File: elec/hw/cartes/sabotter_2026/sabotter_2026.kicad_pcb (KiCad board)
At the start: 4 copper layers, 65 x 100 mm, 124 parts, among them J1 22272021, J10 2-1445051-3, J11 22272051, J12 22272031, J13 3-794630-6, J17 22272061, J3 USB4120-03-C, J5 22272041, J6 3-794630-4, J9 3-794630-4, SW1 PTS525 SK15 SMTR2 LFS, U1 OKI-78SR-3.3/1.5-W36H-C, U2 OKI-78SR-5/1.5-W36H-C, U3 ESP32-S3-WROOM-1, U6 TCAN1042DRQ1, U7 TCA6408ARGTR, U8 SN74LVC1T45DBV

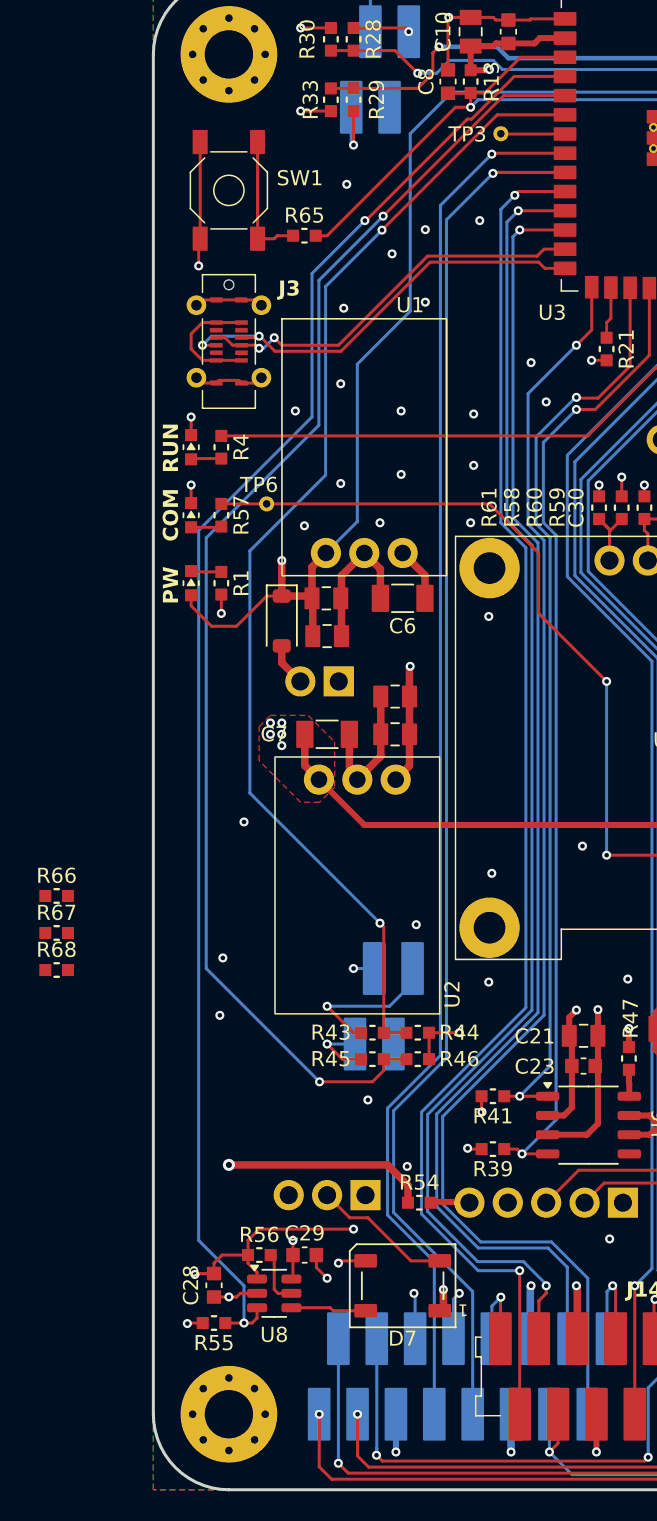
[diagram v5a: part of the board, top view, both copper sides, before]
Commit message: sabotter tof irq routed
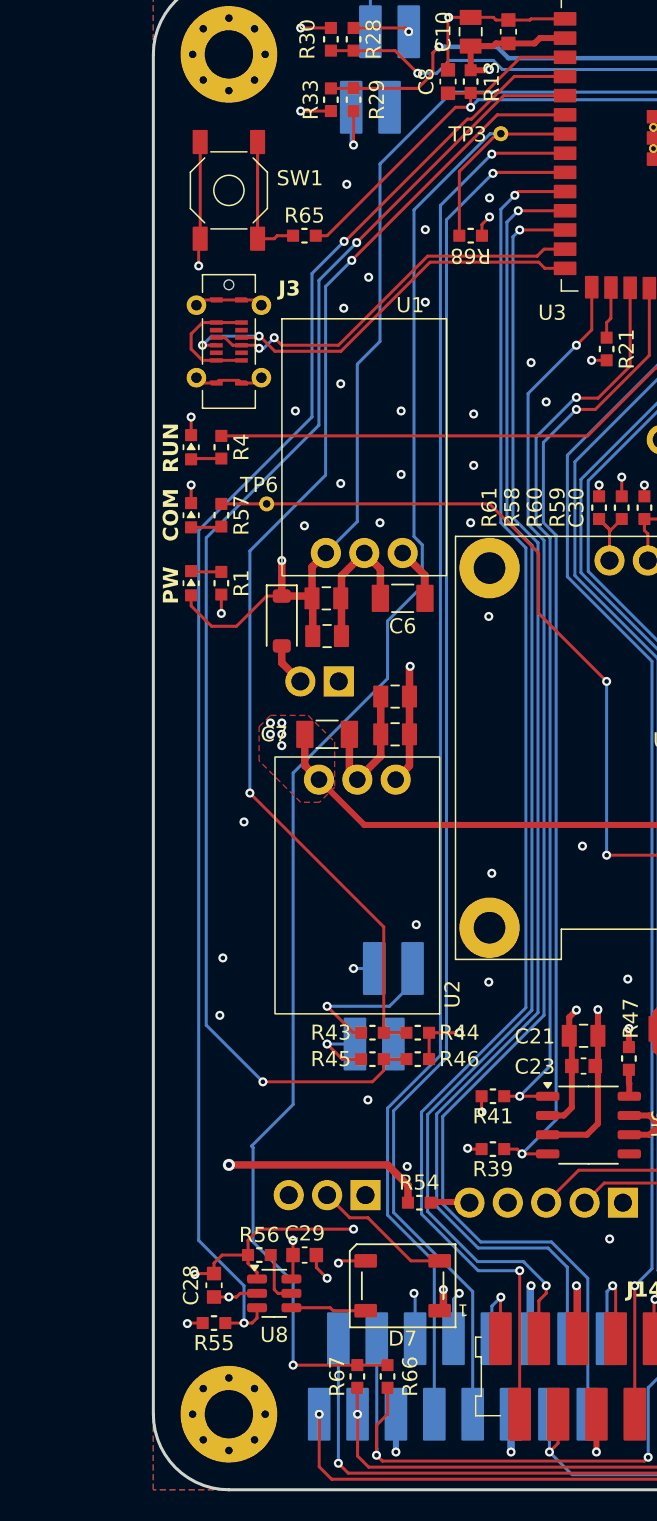
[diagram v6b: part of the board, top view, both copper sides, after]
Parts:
- moved R68 55.8 mm to (131.0, 37.0), turned to 180 degrees
- moved R66 38.6 mm to (125.5, 112.5), turned to 90 degrees
- moved R67 35.5 mm to (123.5, 112.5), turned to 90 degrees
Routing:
- net /motors/tof_irq_3v3: track 4.26 -> 108.9 mm, vias 0 -> 1
- net /motors/irq0_3v3: track 45.8 -> 50.5 mm
- net /interfaces/rx_from_prop_3v3: track 87.4 -> 89.6 mm
- net /motors/irq1_3v3: track 34.1 -> 35.8 mm
- net +3V3: track 91.9 -> 93.4 mm, vias 27 -> 28

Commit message: sabotter corrections wip
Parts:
- added SW2: SLW-713515-2A-SMT-TR, cocotter_others:SLW-713515-2A-SMT-TR, F.Cu at (122.0, 34.0)
- added SW3: SLW-713515-2A-SMT-TR, cocotter_others:SLW-713515-2A-SMT-TR, F.Cu at (170.0, 79.2)
- moved R65 63.2 mm to (164.6, 81.8), turned to 180 degrees
- moved C25 8.61 mm to (169.2, 100.2), turned to 0 degrees
- moved R49 6.64 mm to (169.2, 101.8), turned to 180 degrees
- moved R51 4.00 mm to (169.3, 104.0), turned to 180 degrees
- moved C26 2.94 mm to (169.3, 105.5), turned to 0 degrees
- moved J9 1.25 mm to (162.2, 102.5)
- moved J13 1.00 mm to (149.5, 102.5)
- moved J11 0.50 mm to (135.5, 101.0)
- moved J12 0.50 mm to (122.0, 100.5)
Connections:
- R65 pad 1: Net-(SW1-2) -> Net-(R65-Pad1)
- R65 pad 2: /uc/EN_ESP32_3v3 -> /interfaces/color_select_3v3
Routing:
- net /scl_tof_3v3: track 144.4 -> 136.6 mm
- net /interfaces/ctc_right_3v3: track 17.0 -> 12.9 mm
- net /interfaces/starting_cord_3v3: track 36.7 -> 40.0 mm
- net /motors/DIR_MOT2_3V3: track 84.0 -> 86.7 mm
- net Net-(R65-Pad1): track 0.00 -> 2.00 mm
- net /motors/PWM_MOT2_3V3: track 87.8 -> 89.7 mm
- net /interfaces/ws2812_data_3v3: track 98.9 -> 100.6 mm
- net /interfaces/rx_from_prop_3v3: track 89.6 -> 91.2 mm
- net /interfaces/tx_to_prop_3v3: track 77.2 -> 78.6 mm
- net /interfaces/color_select_3v3: track 30.3 -> 31.6 mm
- net /brake_mot_3v3: track 55.8 -> 57.1 mm
- net /sda_tof_3v3: track 136.3 -> 137.3 mm
- net /interfaces/reset_tof_3v3: track 16.4 -> 17.2 mm
- net /interfaces/enable_tof_3v3: track 14.9 -> 15.5 mm
- net /interfaces/ctc_left_3v3: track 18.3 -> 17.8 mm
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
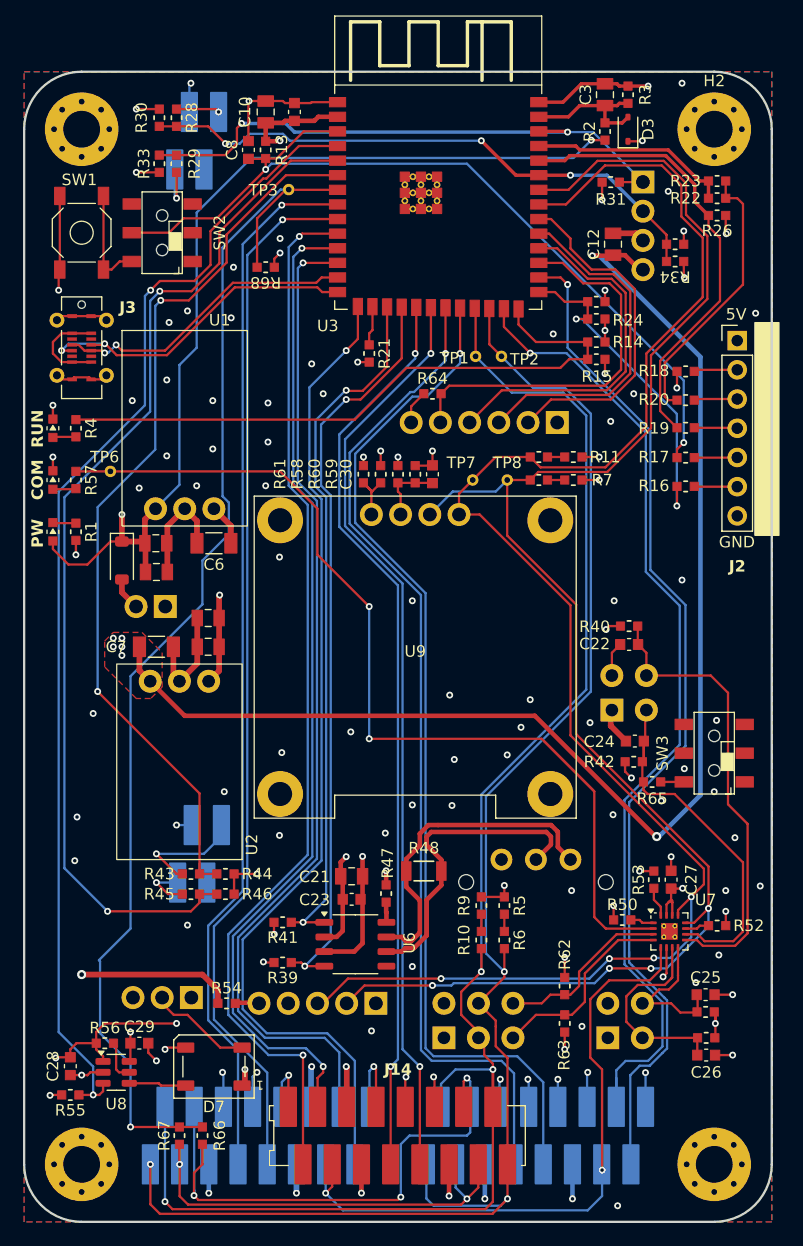
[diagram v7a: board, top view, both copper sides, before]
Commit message: sabotter upodate : switch added to uc reset and color selection
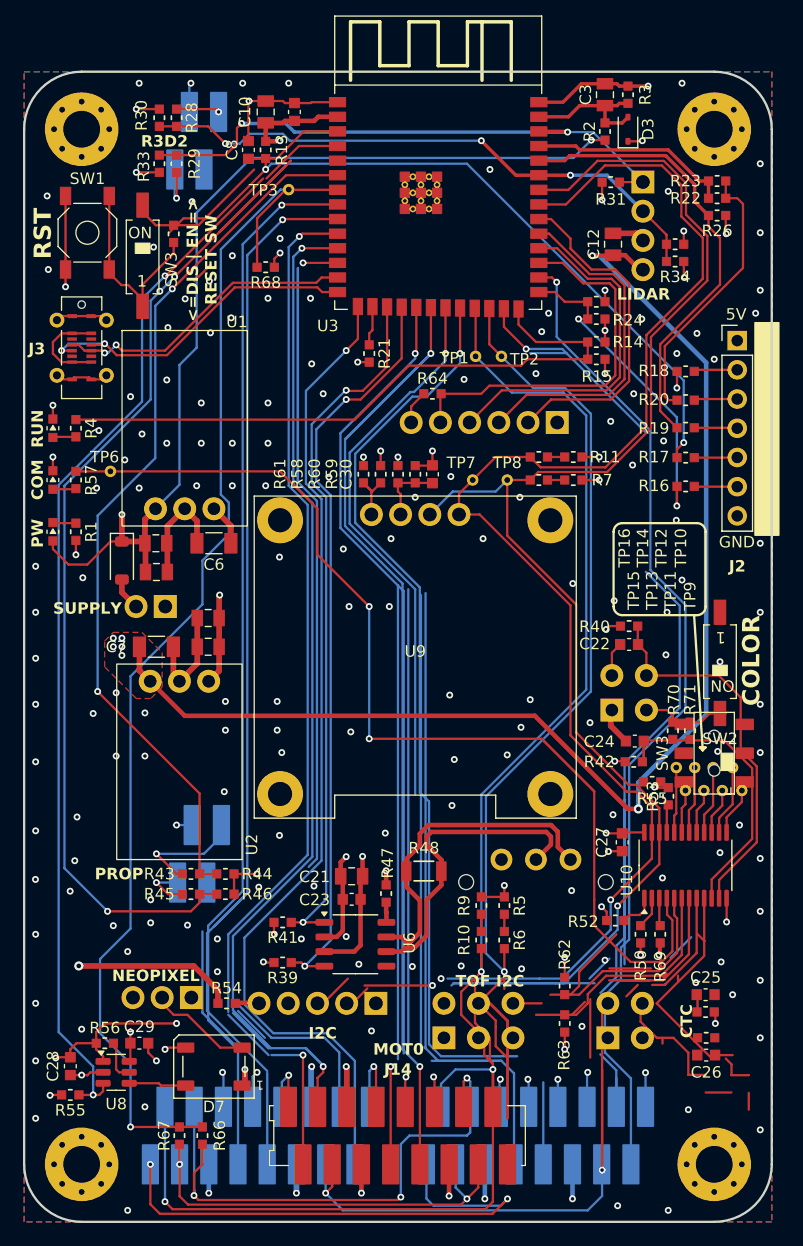
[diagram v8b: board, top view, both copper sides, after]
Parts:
- removed U7: TCA6408ARGTR, cocotter_ic:VQFN-16-1EP_3x3mm_P0.5mm_EP1.1x1.1mm
- added R65: 0R, cocotter_resistor:r0603_reflow, F.Cu at (123.0, 34.1)
- added R69: 0R, cocotter_resistor:r0603_reflow, F.Cu at (165.3, 95.0)
- added R70: 0R, cocotter_resistor:r0603_reflow, F.Cu at (166.4, 77.3)
- added R71: 0R, cocotter_resistor:r0603_reflow, F.Cu at (167.9, 77.3)
- added SW3: DSIC01LSGER, cocotter_others:DIP_SW_SMD-1P, F.Cu at (120.3, 36.0)
- added TP10: TestPoint, cocotter_others:testpoint-THT-0.5mm, F.Cu at (171.6, 80.5)
- added TP11: TestPoint, cocotter_others:testpoint-THT-0.5mm, F.Cu at (170.7, 82.5)
- added TP12: TestPoint, cocotter_others:testpoint-THT-0.5mm, F.Cu at (169.9, 80.5)
- added TP13: TestPoint, cocotter_others:testpoint-THT-0.5mm, F.Cu at (169.1, 82.5)
- added TP14: TestPoint, cocotter_others:testpoint-THT-0.5mm, F.Cu at (168.3, 80.5)
- added TP15: TestPoint, cocotter_others:testpoint-THT-0.5mm, F.Cu at (167.5, 82.5)
- added TP16: TestPoint, cocotter_others:testpoint-THT-0.5mm, F.Cu at (166.7, 80.5)
- added TP9: TestPoint, cocotter_others:testpoint-THT-0.5mm, F.Cu at (172.4, 82.5)
- added U10: PCA9535PW, Package_SO:TSSOP-24_4.4x7.8mm_P0.65mm, F.Cu at (167.5, 89.0)
- R50: value 91k 1% -> 0R
- SW1: footprint cocotter_others:PTS525 SK15 SMTR2 LFS -> cocotter_others:PTS525
- SW2: value SLW-713515-2A-SMT-TR -> DSIC01LSGER; footprint cocotter_others:SLW-713515-2A-SMT-TR -> cocotter_others:DIP_SW_SMD-1P
- moved SW2 61.2 mm to (170.5, 71.4), turned to 180 degrees
- moved R52 8.86 mm to (161.4, 93.8), turned to 0 degrees
- moved R53 7.36 mm to (166.0, 83.0)
- moved C27 5.35 mm to (162.0, 87.0), turned to -90 degrees
- moved R50 2.03 mm to (163.6, 95.0), turned to -90 degrees
- moved SW1 0.50 mm to (115.5, 34.0)
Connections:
- J6 pad 2: /interfaces/color_select_3v3 -> Net-(J6-Pad2)
- R50 pad 1: +3V3 -> Net-(U10-A1)
- R50 pad 2: Net-(U7-~{RESET}) -> GND
- SW2 pad 1: Net-(SW1-2) -> GND
- SW2 pad 2: /uc/EN_ESP32_3v3 -> Net-(SW2-1)
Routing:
- net /motors/ENCODER_A_MOT2_3V3: track 90.0 -> 190.4 mm
- net /motors/ENCODER_B_MOT0_3V3: track 80.3 -> 147.7 mm
- net /motors/ENCODER_B_MOT1_3V3: track 92.0 -> 39.0 mm
- net /motors/ENCODER_A_MOT0_3V3: track 79.7 -> 119.6 mm
- net /motors/DIR_MOT0_3V3: track 87.0 -> 59.4 mm
- net /motors/ENCODER_B_MOT2_3V3: track 88.1 -> 111.1 mm
- net /brake_mot_3v3: track 57.1 -> 79.1 mm
- net /motors/irq0_3v3: track 50.5 -> 68.2 mm
- net /interfaces/sda_3v3: track 143.4 -> 129.9 mm, vias 4 -> 2
- net /interfaces/ctc_left_3v3: track 17.8 -> 30.2 mm
- net /interfaces/ctc_right_3v3: track 12.9 -> 22.7 mm
- net /uc/EN_ESP32_3v3: track 75.3 -> 84.9 mm
- net Net-(U10-A1): track 0.00 -> 9.18 mm
- net Net-(SW1-2): track 9.14 -> 17.8 mm
- net /interfaces/led_com_3v3: track 88.2 -> 96.7 mm
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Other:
- board text added: "<=DIS | EN=> RESET SW"
- board text added: "CAN"
- board text added: "COLOR"
- board text added: "CTC"
- board text added: "GYRO"
- board text added: "I2C"
- board text added: "LIDAR"
- board text added: "MOT0"
- board text added: "MOT1"
- board text added: "MOT2"
- board text added: "NEOPIXEL"
- board text added: "PROP"
- board text added: "R3D2"
- board text added: "RST"
- board text added: "START/COLOR"
- board text added: "SUPPLY"
- board text added: "TOF I2C"
